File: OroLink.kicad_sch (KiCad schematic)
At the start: 6 parts

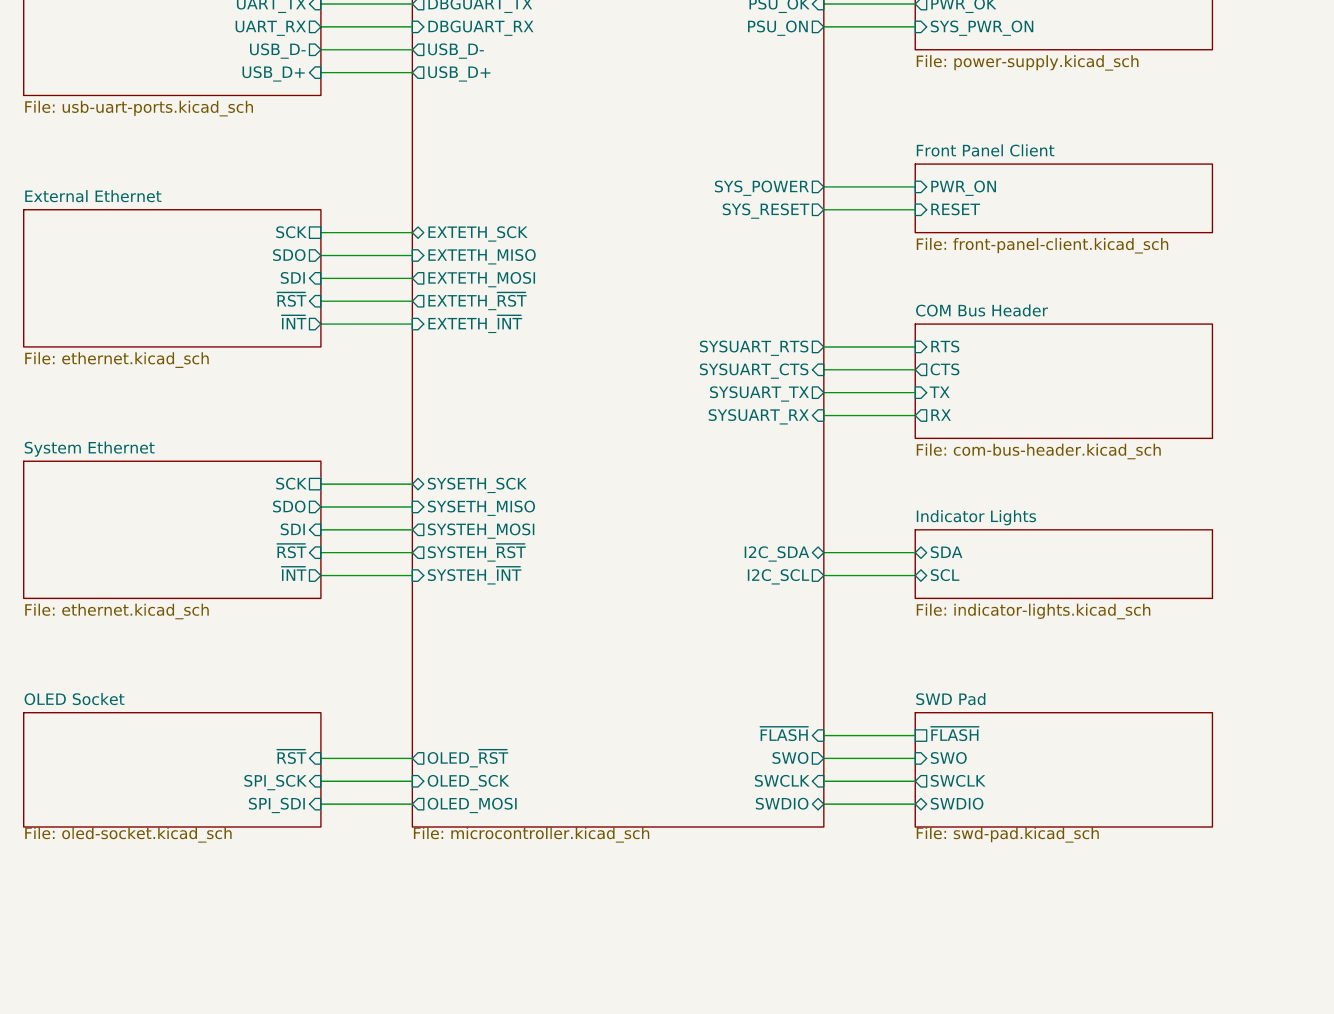
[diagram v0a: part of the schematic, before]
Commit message: switch OLED to 4-wire serial and add CS line to OLED/ethernet chips
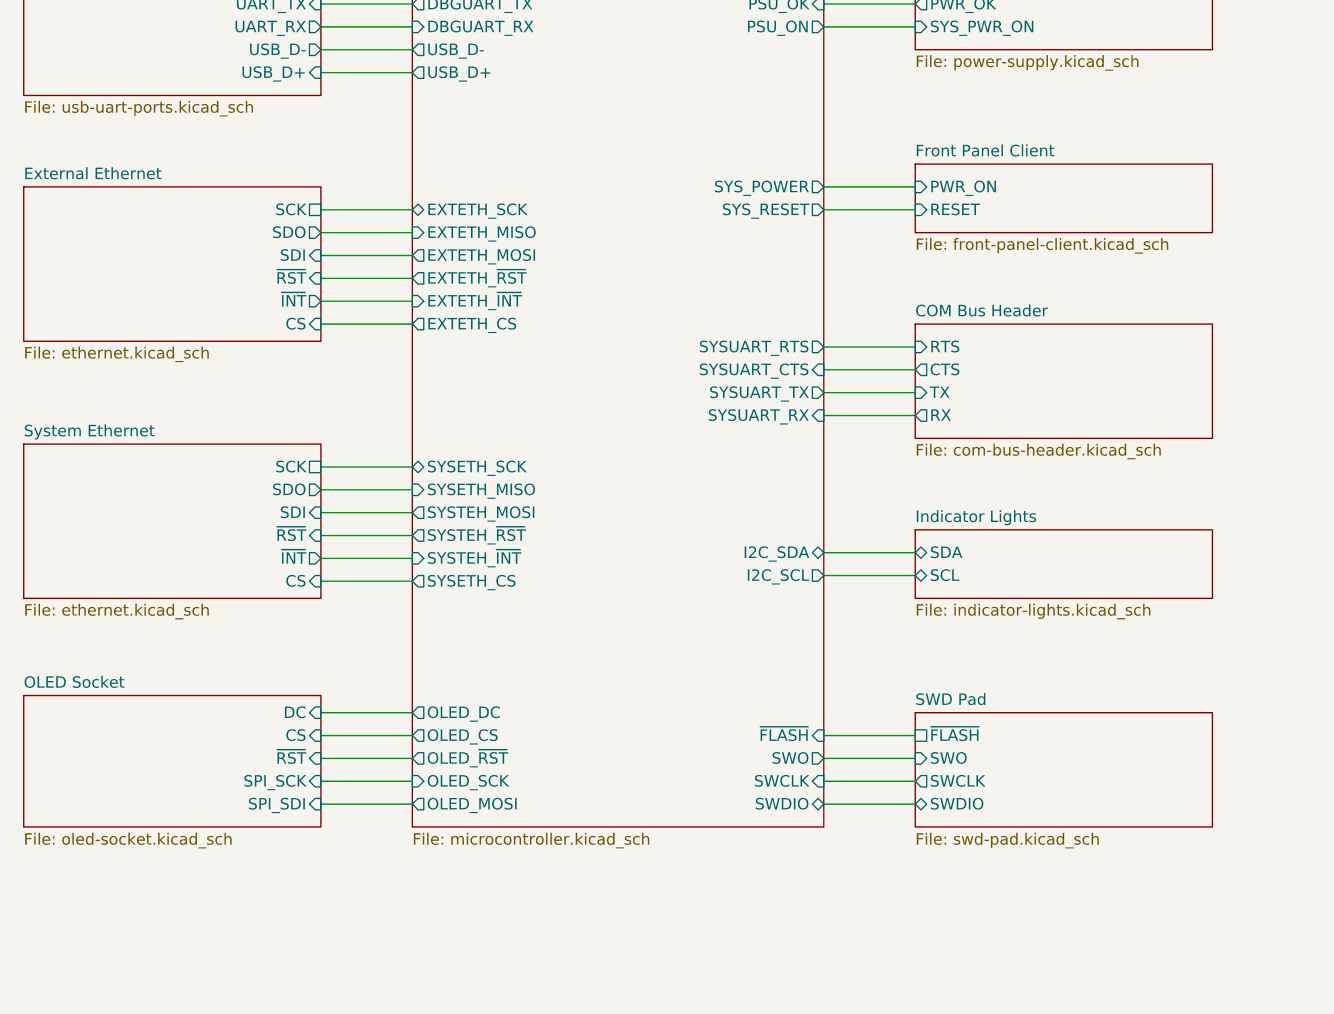
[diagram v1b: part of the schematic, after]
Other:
- sheet External Ethernet ports: added CS; removed none
- sheet Microcontroller ports: added EXTETH_CS, OLED_CS, OLED_DC, SYSETH_CS; removed none
- sheet OLED Socket ports: added CS, DC; removed none
- sheet System Ethernet ports: added CS; removed none

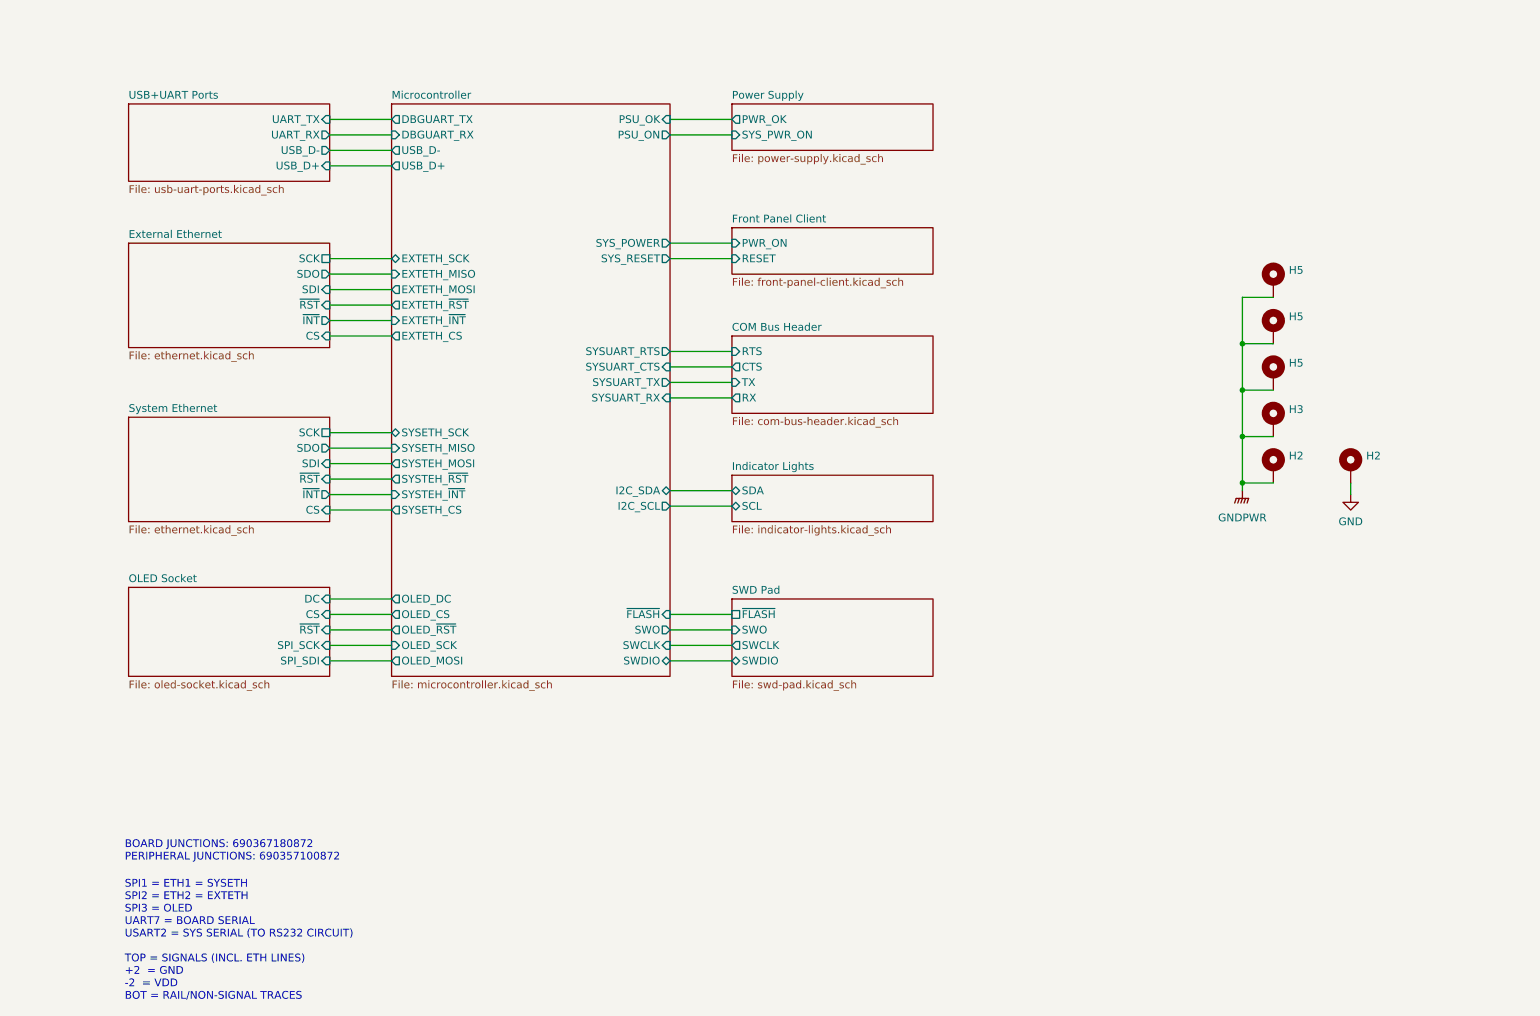
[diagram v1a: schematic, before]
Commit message: remove RS232 DIPs and ESD, and remove redundant header pins
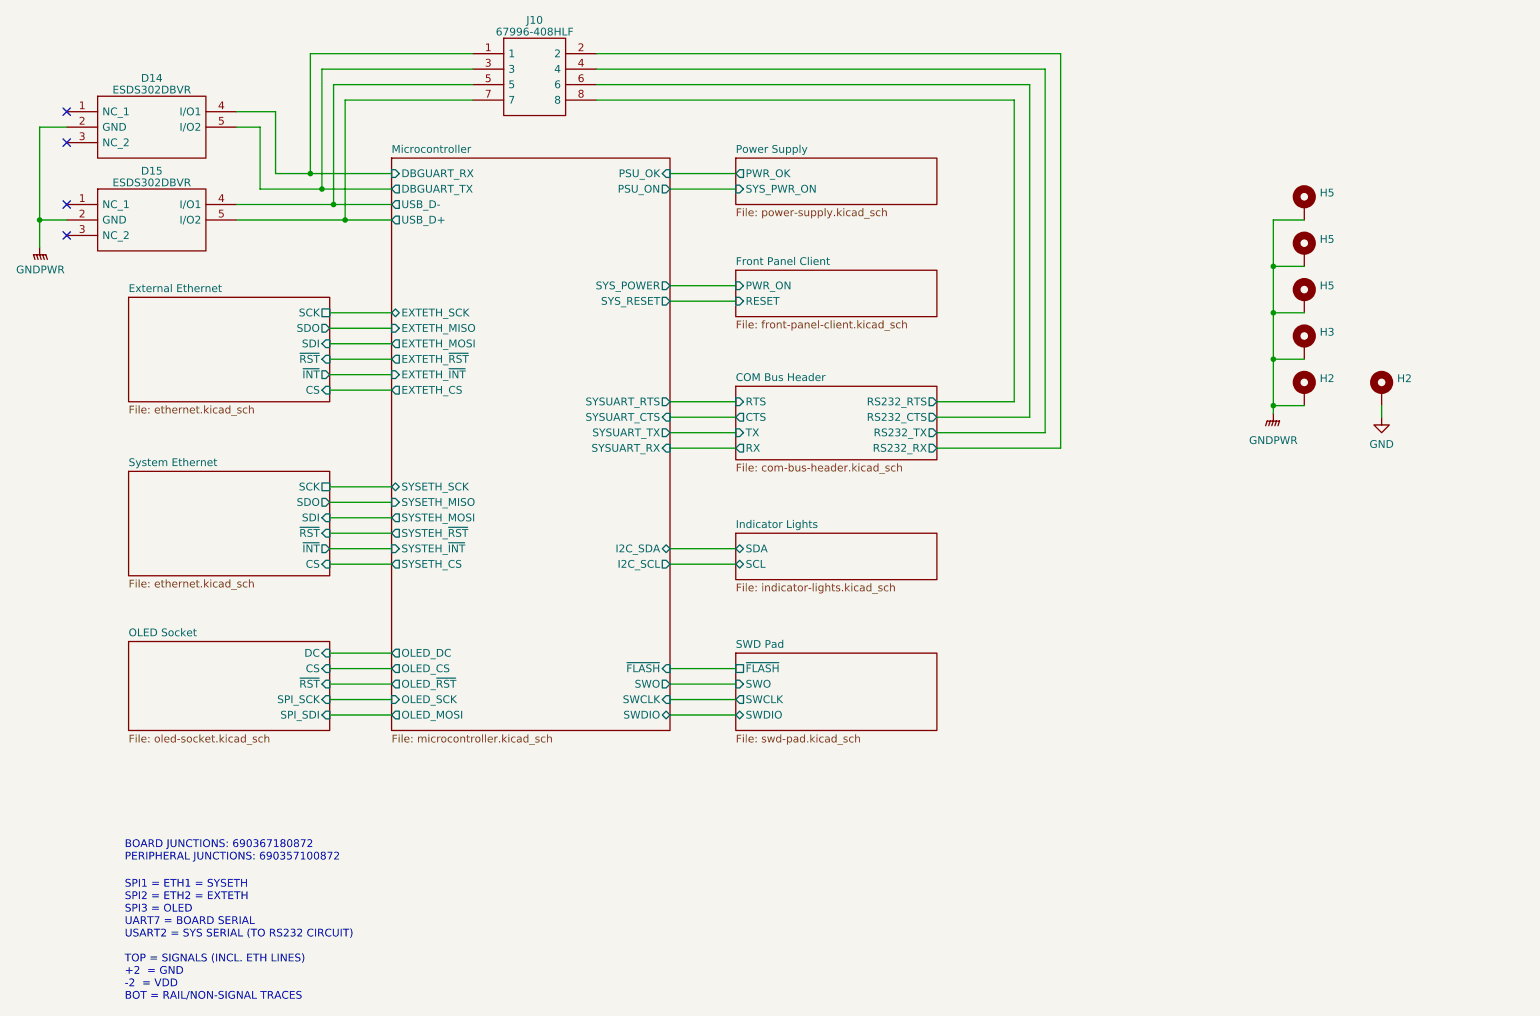
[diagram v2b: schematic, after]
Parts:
- added D14, D15: ESDS302DBVR, SOT95P280X145-5N, symbol SamacSys_Parts:ESDS302DBVR
- added J10: 67996-408HLF, HDRV8W89P254_2X4_1016X483X858P, symbol SamacSys_Parts:67996-408HLF
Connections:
- net GNDPWR: now also D14.2 (GND), D15.2 (GND)
- net Microcontroller/DBGUART_RX: now also D14.4 (I/O1), J10.1
- net Microcontroller/DBGUART_TX: now also D14.5 (I/O2), J10.3
- net Microcontroller/USB_D+: now also D15.5 (I/O2), J10.7
- net Microcontroller/USB_D-: now also D15.4 (I/O1), J10.5
- new net COM Bus Header/RS232_CTS: J10.6
- new net COM Bus Header/RS232_RTS: J10.8
- new net COM Bus Header/RS232_RX: J10.2
- new net COM Bus Header/RS232_TX: J10.4
- no-connect marks 0 -> 4
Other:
- removed sheet USB+UART Ports
- sheet COM Bus Header ports: added RS232_CTS, RS232_RTS, RS232_RX, RS232_TX; removed none
- moved on the sheet: H2, H3, H5

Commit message: add GND/GNDPWR jumper for non-conductive chassis
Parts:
- added B2: 382811-8, symbol Oro:BOM Part
- added J7: 10129378-902003BLF, HDRV2W67P0X254_1X2_508X241X1082P, symbol SamacSys_Parts:10129378-902003BLF
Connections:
- net GND: now also J7.1
- net GNDPWR: now also J7.2
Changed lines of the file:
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@@
+    (stroke (width 0) (type default))
+  )
+  (wire (pts (xy 227.965 124.46) (xy 234.95 124.46))
     (stroke (width 0) (type default))
   )
@@
     (stroke (width 0) (type default))
   )
+  (wire (pts (xy 234.95 124.46) (xy 234.95 125.095))
+    (stroke (width 0) (type default))
+  )
   (wire (pts (xy 193.675 97.79) (xy 193.675 33.02))
     (stroke (width 0) (type default))
@@
     (stroke (width 0) (type default))
   )
+  (wire (pts (xy 222.25 131.445) (xy 234.95 131.445))
+    (stroke (width 0) (type default))
+  )
   (wire (pts (xy 73.66 106.68) (xy 83.82 106.68))
     (stroke (width 0) (type default))
@@
     (stroke (width 0) (type default))
   )
+  (wire (pts (xy 222.25 128.905) (xy 227.965 128.905))
+    (stroke (width 0) (type default))
+  )
   (wire (pts (xy 191.135 95.25) (xy 191.135 35.56))
     (stroke (width 0) (type default))
@@
   )
   (wire (pts (xy 74.295 57.785) (xy 83.82 57.785))
+    (stroke (width 0) (type default))
+  )
+  (wire (pts (xy 227.965 128.905) (xy 227.965 124.46))
     (stroke (width 0) (type default))
   )
@@
     )
   )
+  (symbol (lib_id "power:GND") (at 234.95 125.095 0) (unit 1)
+    (in_bom yes) (on_board yes) (dnp no)
+    (property "Reference" "#PWR025" (at 234.95 131.445 0)
+      (effects (font (size 1.27 1.27)) hide)
+    )
+    (property "Value" "GND" (at 234.95 129.54 0)
+      (effects (font (size 1.27 1.27)))
+    )
+    (property "Footprint" "" (at 234.95 125.095 0)
+      (effects (font (size 1.27 1.27)) hide)
+    )
+    (property "Datasheet" "" (at 234.95 125.095 0)
+      (effects (font (size 1.27 1.27)) hide)
+    )
+    (pin "1")
+    (instances
+      (project "OroLink"
+        (path "/e89dcd22-1250-4a5b-b778-1c95a0dd623d/f955395e-bf1a-4ef3-9cfe-ec9d49f66988"
+          (reference "#PWR025") (unit 1)
+        )
+        (path "/e89dcd22-1250-4a5b-b778-1c95a0dd623d"
+          (reference "#PWR043") (unit 1)
+        )
+      )
+    )
+  )
   (symbol (lib_id "SamacSys_Parts:ESDS302DBVR") (at 30.48 57.785 0) (unit 1)
     (in_bom yes) (on_board yes) (dnp no)
@@
     )
   )
+  (symbol (lib_id "power:GNDPWR") (at 234.95 131.445 0) (unit 1)
+    (in_bom yes) (on_board yes) (dnp no)
+    (property "Reference" "#PWR030" (at 234.95 136.525 0)
+      (effects (font (size 1.27 1.27)) hide)
+    )
+    (property "Value" "GNDPWR" (at 234.95 135.89 0)
+      (effects (font (size 1.27 1.27)))
+    )
+    (property "Footprint" "" (at 234.95 132.715 0)
+      (effects (font (size 1.27 1.27)) hide)
+    )
+    (property "Datasheet" "" (at 234.95 132.715 0)
+      (effects (font (size 1.27 1.27)) hide)
+    )
+    (pin "1")
+    (instances
+      (project "OroLink"
+        (path "/e89dcd22-1250-4a5b-b778-1c95a0dd623d"
+          (reference "#PWR030") (unit 1)
+        )
+        (path "/e89dcd22-1250-4a5b-b778-1c95a0dd623d/f955395e-bf1a-4ef3-9cfe-ec9d49f66988"
+          (reference "#PWR024") (unit 1)
+        )
+      )
+    )
+  )
   (symbol (lib_id "Mechanical:MountingHole_Pad") (at 246.38 88.265 0) (unit 1)
     (in_bom no) (on_board yes) (dnp no)
@@
   (symbol (lib_id "power:GNDPWR") (at 26.035 64.77 0) (mirror y) (unit 1)
     (in_bom yes) (on_board yes) (dnp no) (fields_autoplaced)
-    (property "Reference" "#PWR073" (at 26.035 69.85 0)
+    (property "Reference" "#PWR021" (at 26.035 69.85 0)
       (effects (font (size 1.27 1.27)) hide)
     )
@@
         (path "/e89dcd22-1250-4a5b-b778-1c95a0dd623d"
           (reference "#PWR021") (unit 1)
+        )
+      )
+    )
+  )
+  (symbol (lib_id "SamacSys_Parts:10129378-902003BLF") (at 222.25 128.905 0) (mirror y) (unit 1)
+    (in_bom yes) (on_board yes) (dnp no)
+    (property "Reference" "J7" (at 212.09 123.19 0)
+      (effects (font (size 1.27 1.27)))
+    )
+    (property "Value" "10129378-902003BLF" (at 212.09 125.095 0)
+      (effects (font (size 1.27 1.27)))
+    )
+    (property "Footprint" "HDRV2W67P0X254_1X2_508X241X1082P" (at 205.74 126.365 0)
+      (effects (font (size 1.27 1.27)) (justify left) hide)
+    )
+    (property "Datasheet" "https://cdn.amphenol-cs.com/media/wysiwyg/files/drawing/10129378.pdf" (at 205.74 128.905 0)
+      (effects (font (size 1.27 1.27)) (justify left) hide)
+    )
+    (property "Description" "EconoStik 2.54mm, Board to Board Connector, Unshrouded Verticl Header, Through Hole, Single Row, 2 Positions, 2.54 mm (0.100in) Pitch." (at 205.74 131.445 0)
+      (effects (font (size 1.27 1.27)) (justify left) hide)
+    )
+    (property "Height" "10.82" (at 205.74 133.985 0)
+      (effects (font (size 1.27 1.27)) (justify left) hide)
+    )
+    (property "Manufacturer_Name" "Amphenol Communication Solutions" (at 205.74 136.525 0)
+      (effects (font (size 1.27 1.27)) (justify left) hide)
+    )
+    (property "Manufacturer_Part_Number" "10129378-902003BLF" (at 205.74 139.065 0)
+      (effects (font (size 1.27 1.27)) (justify left) hide)
+    )
+    (property "Mouser Part Number" "649-1012937890203BLF" (at 205.74 141.605 0)
+      (effects (font (size 1.27 1.27)) (justify left) hide)
+    )
+    (property "Mouser Price/Stock" "https://www.mouser.co.uk/ProductDetail/Amphenol-FCI/10129378-902003BLF?qs=0lQeLiL1qyZU%252BgRaQ8FKPg%3D%3D" (at 205.74 144.145 0)
+      (effects (font (size 1.27 1.27)) (justify left) hide)
+    )
+    (property "Arrow Part Number" "" (at 205.74 146.685 0)
+      (effects (font (size 1.27 1.27)) (justify left) hide)
+    )
+    (property "Arrow Price/Stock" "" (at 205.74 149.225 0)
+      (effects (font (size 1.27 1.27)) (justify left) hide)
+    )
+    (property "Note" "FOR NON-CONDUCTIVE CHASSIS" (at 212.09 135.89 0)
+      (effects (font (size 1.27 1.27)))
+    )
+    (pin "1")
+    (pin "2")
+    (instances
+      (project "OroLink"
+        (path "/e89dcd22-1250-4a5b-b778-1c95a0dd623d"
+          (reference "J2") (unit 1)
         )
       )
@@
         )
       )
+    )
+  )
+  (symbol (lib_id "Oro:BOM Part") (at 251.46 130.175 0) (unit 1)
+    (in_bom yes) (on_board no) (dnp no)
+    (property "Reference" "B2" (at 253.365 129.5313 0)
+      (effects (font (size 1.27 1.27)) (justify left) hide)
+    )
+    (property "Value" "382811-8" (at 254 131.445 0)
+      (effects (font (size 1.27 1.27)) (justify left))
+    )
+    (property "Footprint" "" (at 251.46 130.175 0)
+      (effects (font (size 1.27 1.27)) hide)
+    )
+    (property "Datasheet" "https://www.te.com/commerce/DocumentDelivery/DDEController?Action=srchrtrv&DocNm=382811&DocType=Customer+Drawing&DocLang=English&PartCntxt=382811-8&DocFormat=pdf" (at 251.46 130.175 0)
+      (effects (font (size 1.27 1.27)) hide)
+    )
+    (property "Sim.Enable" "0" (at 251.46 130.175 0)
+      (effects (font (size 1.27 1.27)) hide)
+    )
+    (property "Manufacturer_Part_Number" "382811-8" (at 251.46 130.175 0)
+      (effects (font (size 1.27 1.27)) hide)
+    )
+    (property "Mouser Part Number" "571-3828118" (at 251.46 130.175 0)
+      (effects (font (size 1.27 1.27)) hide)
+    )
+    (property "Note" "JUMPER SHUNT" (at 254 130.175 0)
+      (effects (font (size 1.27 1.27)) (justify left bottom))
+    )
+    (instances
+      (project "Oro Testbed v2"
+        (path "/3d0fc623-63eb-45e5-a304-e470d9b3a173"
+          (reference "B2") (unit 1)
+        )
+        (path "/3d0fc623-63eb-45e5-a304-e470d9b3a173/7310340d-2c15-4c32-b17d-f4923dae9f8e"
+          (reference "B2") (unit 1)
+        )
+      )
+      (project "OroLink"
+        (path "/e89dcd22-1250-4a5b-b778-1c95a0dd623d/1b3eede1-74b0-4c0b-b4f1-7ec1bfc1f54f"
+          (reference "B3") (unit 1)
+        )
+        (path "/e89dcd22-1250-4a5b-b778-1c95a0dd623d"
+          (reference "B4") (unit 1)
+        )
+      )
